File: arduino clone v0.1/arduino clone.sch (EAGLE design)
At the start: 24 parts, among them J202 FTDI Breakout Header, U101 ATMEGA328P_TQFP, U201 CH340G

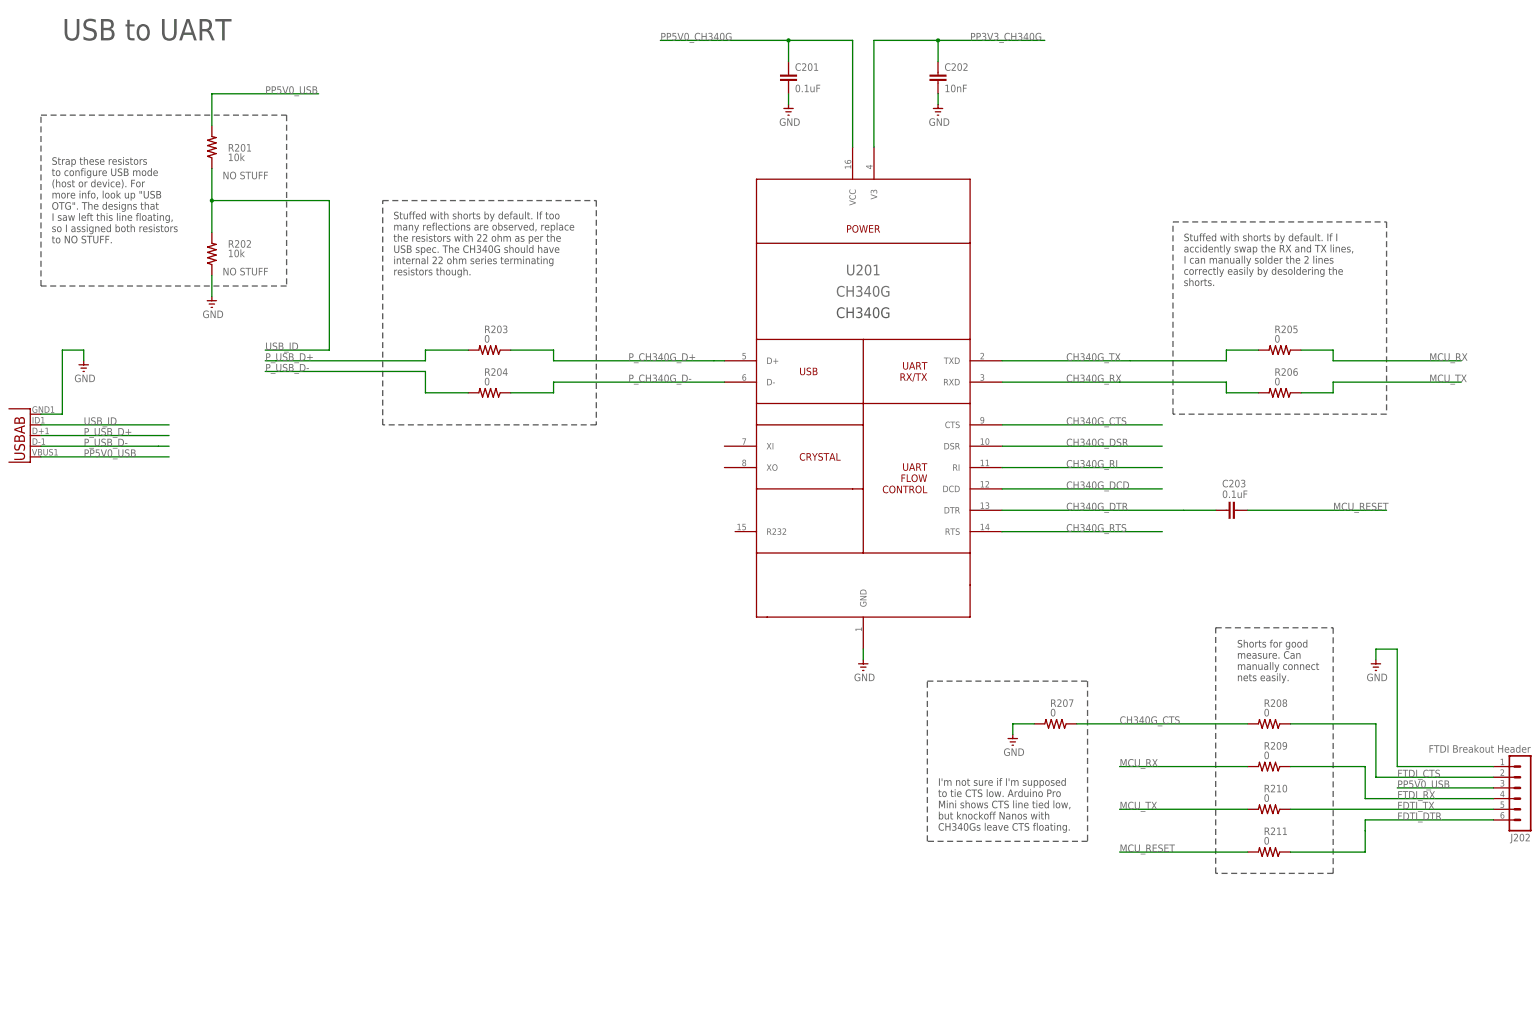
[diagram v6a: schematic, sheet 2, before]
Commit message: add strapping resistors on CH340G_R323 pin
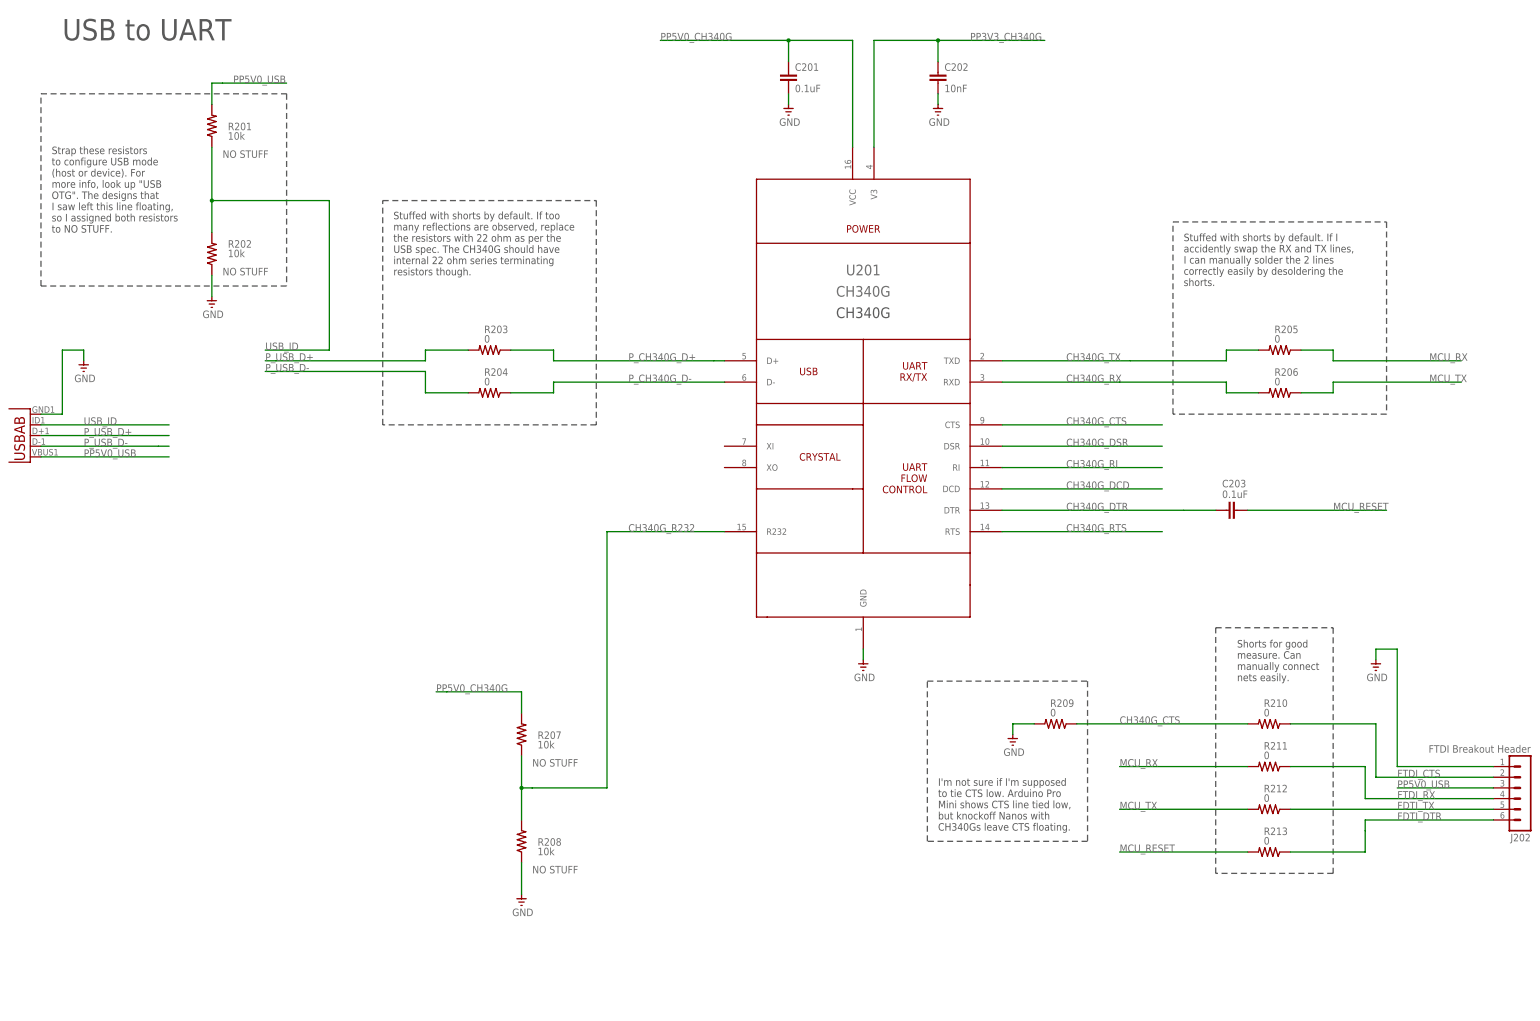
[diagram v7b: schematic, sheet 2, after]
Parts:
- added R212, R213: 0, adafruit:R-US_R0805
- R207, R208: value 0 -> 10k; STUFF (none) -> NO STUFF
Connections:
- new net CH340G_R232: U201.R232
- new net N$1: R207.1, R208.2
- net CH340G_CTS: now also R209.1, R210.2; no longer R207.1, R208.2
- net FDTI_DTR: now also R213.1; no longer R211.1
- net FDTI_TX: now also R212.1; no longer R210.1
- net FTDI_CTS: now also R210.1; no longer R208.1
- net FTDI_RX: now also R211.1; no longer R209.1
- net GND: now also R208.1, R209.2; no longer R207.2
- net MCU_RESET: now also R213.2; no longer R211.2
- net MCU_RX: now also R211.2; no longer R209.2
- net MCU_TX: now also R212.2; no longer R210.2
- net PP5V0_CH340G: now also R207.2
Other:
- moved on the sheet: R201, R207, R208, R209, R210, R211

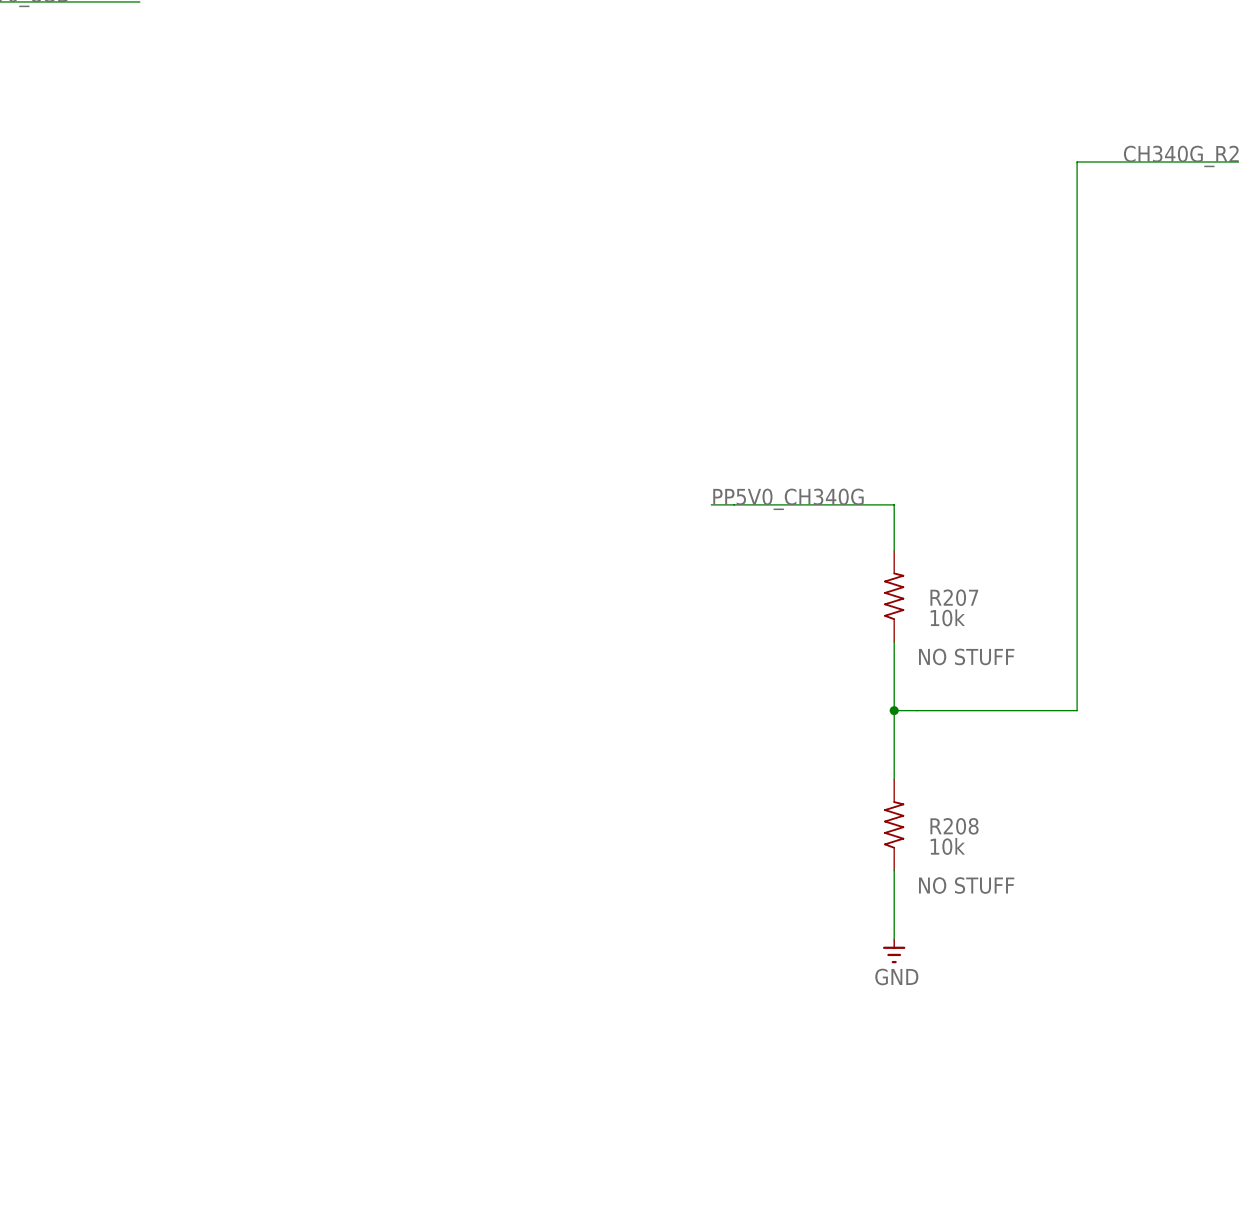
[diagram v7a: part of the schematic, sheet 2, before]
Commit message: ad notes to R232 strapping resistors
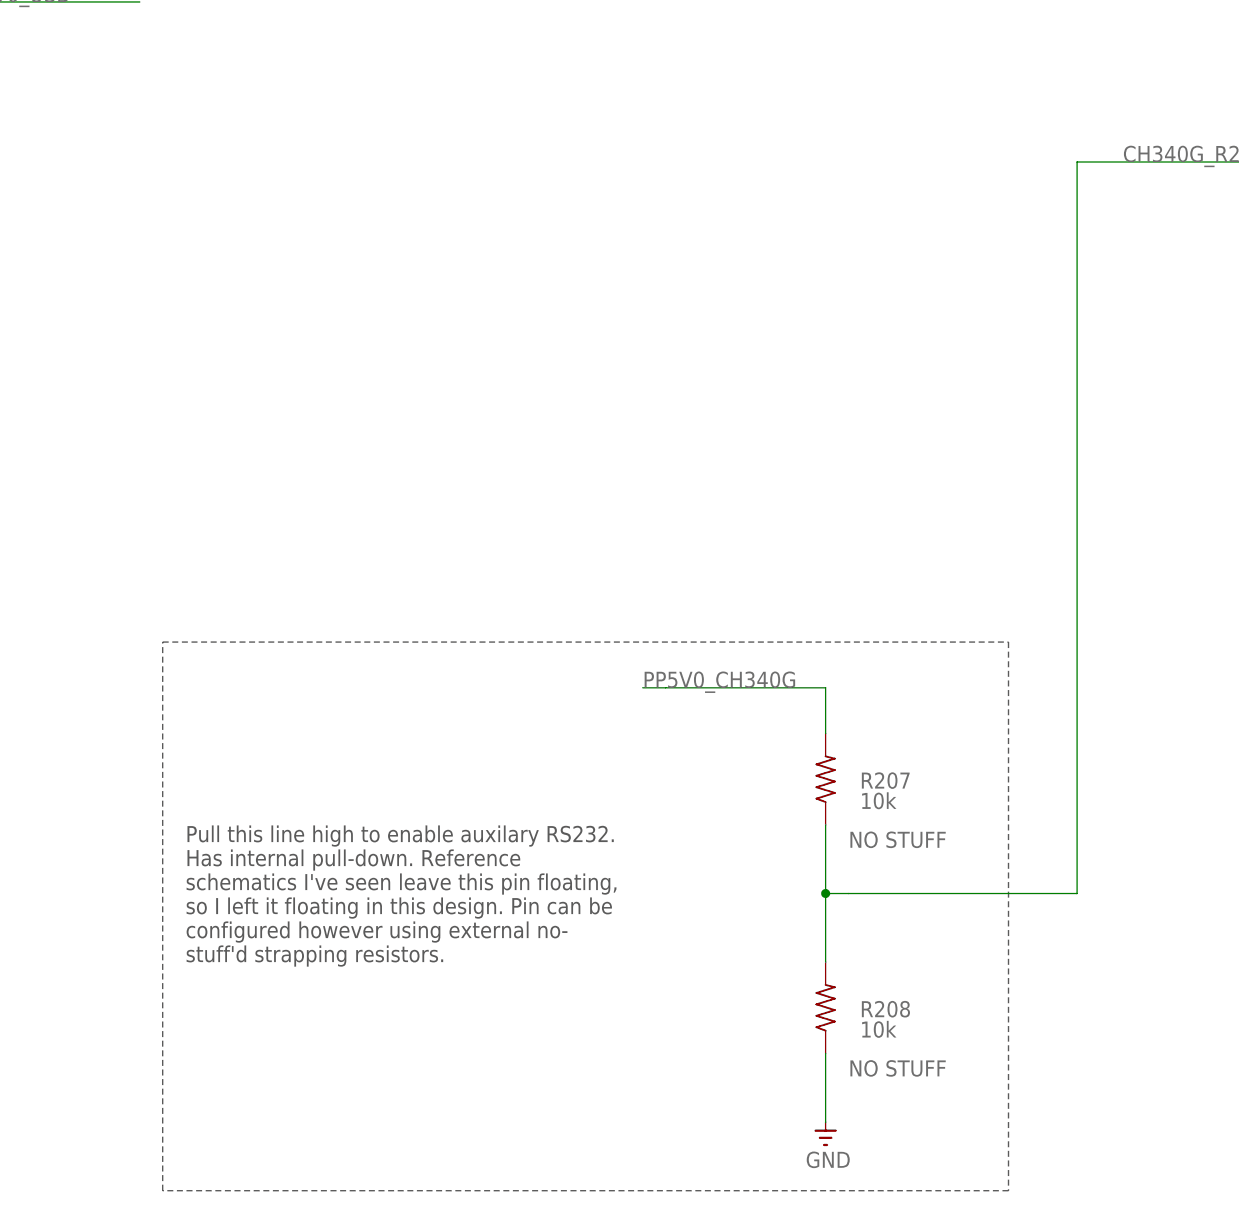
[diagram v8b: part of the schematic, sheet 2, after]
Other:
- note added: "Pull this line high to enable auxilary RS232. Has internal pull-down. Reference schematics I've seen leave this pin floating, so I left it floating in this design. Pin can be configured however using external no- stuff'd strapping resistors."
- moved on the sheet: R207, R208
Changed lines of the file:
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@@
 <wire x1="231.14" y1="48.26" x2="231.14" y2="86.36" width="0.1524" layer="97" style="shortdash"/>
 <wire x1="231.14" y1="86.36" x2="269.24" y2="86.36" width="0.1524" layer="97" style="shortdash"/>
+<text x="55.88" y="33.02" size="1.778" layer="97">Pull this line high to enable auxilary RS232.
+Has internal pull-down. Reference
+schematics I've seen leave this pin floating,
+so I left it floating in this design. Pin can be
+configured however using external no-
+stuff'd strapping resistors.</text>
+<wire x1="147.32" y1="68.58" x2="147.32" y2="7.62" width="0.1524" layer="97" style="shortdash"/>
+<wire x1="147.32" y1="7.62" x2="53.34" y2="7.62" width="0.1524" layer="97" style="shortdash"/>
+<wire x1="53.34" y1="7.62" x2="53.34" y2="68.58" width="0.1524" layer="97" style="shortdash"/>
+<wire x1="53.34" y1="68.58" x2="147.32" y2="68.58" width="0.1524" layer="97" style="shortdash"/>
 </plain>
 <instances>
@@
 <attribute name="VALUE" x="311.15" y="47.498" size="1.778" layer="96"/>
 </instance>
-<instance part="R207" gate="G$1" x="134.62" y="73.66" smashed="yes" rot="R90">
-<attribute name="NAME" x="138.43" y="72.6186" size="1.778" layer="95"/>
-<attribute name="VALUE" x="138.43" y="70.358" size="1.778" layer="96"/>
-<attribute name="STUFF" x="137.16" y="66.04" size="1.778" layer="96"/>
-</instance>
-<instance part="R208" gate="G$1" x="134.62" y="48.26" smashed="yes" rot="R90">
-<attribute name="NAME" x="138.43" y="47.2186" size="1.778" layer="95"/>
-<attribute name="VALUE" x="138.43" y="44.958" size="1.778" layer="96"/>
-<attribute name="STUFF" x="137.16" y="40.64" size="1.778" layer="96"/>
-</instance>
-<instance part="GND14" gate="1" x="134.62" y="33.02" smashed="yes">
-<attribute name="VALUE" x="132.3975" y="30.48" size="1.778" layer="96"/>
+<instance part="R207" gate="G$1" x="127" y="53.34" smashed="yes" rot="R90">
+<attribute name="NAME" x="130.81" y="52.2986" size="1.778" layer="95"/>
+<attribute name="VALUE" x="130.81" y="50.038" size="1.778" layer="96"/>
+<attribute name="STUFF" x="129.54" y="45.72" size="1.778" layer="96"/>
+</instance>
+<instance part="R208" gate="G$1" x="127" y="27.94" smashed="yes" rot="R90">
+<attribute name="NAME" x="130.81" y="26.8986" size="1.778" layer="95"/>
+<attribute name="VALUE" x="130.81" y="24.638" size="1.778" layer="96"/>
+<attribute name="STUFF" x="129.54" y="20.32" size="1.778" layer="96"/>
+</instance>
+<instance part="GND14" gate="1" x="127" y="12.7" smashed="yes">
+<attribute name="VALUE" x="124.7775" y="10.16" size="1.778" layer="96"/>
 </instance>
 </instances>
@@
 <segment>
 <pinref part="R207" gate="G$1" pin="2"/>
-<wire x1="134.62" y1="78.74" x2="134.62" y2="83.82" width="0.1524" layer="91"/>
-<wire x1="134.62" y1="83.82" x2="116.84" y2="83.82" width="0.1524" layer="91"/>
-<label x="114.3" y="83.82" size="1.778" layer="95"/>
-<wire x1="116.84" y1="83.82" x2="114.3" y2="83.82" width="0.1524" layer="91"/>
+<wire x1="127" y1="58.42" x2="127" y2="63.5" width="0.1524" layer="91"/>
+<wire x1="127" y1="63.5" x2="109.22" y2="63.5" width="0.1524" layer="91"/>
+<label x="106.68" y="63.5" size="1.778" layer="95"/>
+<wire x1="109.22" y1="63.5" x2="106.68" y2="63.5" width="0.1524" layer="91"/>
 </segment>
 </net>
@@
 <pinref part="GND14" gate="1" pin="GND"/>
 <pinref part="R208" gate="G$1" pin="1"/>
-<wire x1="134.62" y1="35.56" x2="134.62" y2="43.18" width="0.1524" layer="91"/>
+<wire x1="127" y1="15.24" x2="127" y2="22.86" width="0.1524" layer="91"/>
 </segment>
 </net>
@@
 <pinref part="U201" gate="G$1" pin="R232"/>
 <wire x1="182.88" y1="121.92" x2="154.94" y2="121.92" width="0.1524" layer="91"/>
-<wire x1="154.94" y1="121.92" x2="154.94" y2="60.96" width="0.1524" layer="91"/>
+<wire x1="154.94" y1="121.92" x2="154.94" y2="40.64" width="0.1524" layer="91"/>
 <label x="160.02" y="121.92" size="1.778" layer="95"/>
 </segment>
@@
 <pinref part="R208" gate="G$1" pin="2"/>
 <pinref part="R207" gate="G$1" pin="1"/>
-<wire x1="134.62" y1="53.34" x2="134.62" y2="60.96" width="0.1524" layer="91"/>
-<wire x1="134.62" y1="60.96" x2="134.62" y2="68.58" width="0.1524" layer="91"/>
-<wire x1="134.62" y1="60.96" x2="137.16" y2="60.96" width="0.1524" layer="91"/>
-<wire x1="137.16" y1="60.96" x2="154.94" y2="60.96" width="0.1524" layer="91"/>
-<junction x="134.62" y="60.96"/>
-</segment>
-</net>
+<wire x1="127" y1="33.02" x2="127" y2="40.64" width="0.1524" layer="91"/>
+<wire x1="127" y1="40.64" x2="127" y2="48.26" width="0.1524" layer="91"/>
+<wire x1="127" y1="40.64" x2="129.54" y2="40.64" width="0.1524" layer="91"/>
+<wire x1="129.54" y1="40.64" x2="154.94" y2="40.64" width="0.1524" layer="91"/>
+<junction x="127" y="40.64"/>
+</segment>
+</net>
